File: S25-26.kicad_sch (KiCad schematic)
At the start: 122 parts, among them IC1 CMV4000-3E5M0PN, IC10 MT29F2G01ABAGDWB-IT_G_TR, IC13 DS90LV011AHMF_NOPB, IC2 XMC7200D-E272K8384AA, IC3 DS90LV048ATM_NOPB, IC4 DS90LV048ATM_NOPB, IC5 DS90LV048ATM_NOPB, IC6 NCV317BD2TR4G, IC7 MXL86110I-AQB-R, IC9 MT29F2G01ABAGDWB-IT_G_TR, J1 RJ45_RB1-125B8G1A, J2 DC_IN_PADS, J3 Conn_01x02_Pin, J4 Conn_01x04_Pin, Q2 ZXT849K, U1 TPS73601DBV, U2 TPS73601DBV, Y1 DSC1101DM2-012.0000

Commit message: Implementing Global Labels
Swapping generic I/O labels for global labels to help provide clarity in the schematic. Completed Supply Decoupling Caps, Temp. Sensing, Voltage Regulation, and part of Core Ext. Regulator
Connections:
- net DC_LINE_IN: no longer C36.1, Cin4.1, D1.1 (K), IC6.3 (VIN)
- net EXT_PS_CTL1 renamed XMC_VCCD
- new net DC_LINE_IN_28V: C36.1, Cin4.1, D1.1 (K), IC6.3 (VIN)
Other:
- moved on the sheet: C65, Q2, R2, R4, TR2, VCORE

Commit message: Reverted schematic to hierarchical structure.
The following connections are known to be floating:
FRAME_REQ
CMOS_RESET_N
CMOS_CLK_OUT
ETH0_RX_ER
ETH0_ETH_TSU_TIMER_CMP_VAL
ETH0_TX_ER
ETH0_REF_CLK
LVDS_RECV_EN
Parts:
- removed 2v1, 3v0, 3v3, VCORE, XRES: TestPoint, TestPoint:TestPoint_Pad_D1.0mm, symbol Connector:TestPoint
- removed C11, C14, C19, C20, C22: 0.1uF, symbol Device:C_Polarized
- removed C12, C17, C18, C21: 1nF, symbol Device:C_Polarized
- removed C13: 15pF, symbol Device:C
- removed C15: 0.1uF, symbol Device:C
- removed C16: 10uF, symbol Device:C_Small
- removed C23: 0.1F, symbol Device:C
- removed C36, CAdj4: 10uF, symbol Device:C_Polarized
- removed C37, C38, C39, C40, C41, C42, C44, C45, C46, C48, C49, C51, C52, C53, C54, C56, C59, C62, C64: 0.1uF, symbol Device:C_Small
- removed C43, C47, C50, C55, C58: 1uF, symbol Device:C_Small
- removed C57, C60: 10nF, symbol Device:C_Small
- removed C61, C63: 2.2uF, symbol Device:C_Small
- removed C65: 10uF, symbol Device:C
- removed CAdj5, CAdj6: 10nF, symbol Device:C_Polarized
- removed Cin4, Cin5, Cin6, Co4, Co5, Co6: 1uF, symbol Device:C_Polarized
- removed D1, D2: 1N4002, Diode_THT:D_DO-41_SOD81_P10.16mm_Horizontal, symbol Diode:1N4002
- removed IC10, IC9: MT29F2G01ABAGDWB-IT_G_TR, SON127P800X600X65-8N, symbol SamacSys_Parts:MT29F2G01ABAGDWB-IT_G_TR
- removed IC13: DS90LV011AHMF_NOPB, SOT95P280X145-5N, symbol SamacSys_Parts:DS90LV011AHMF_NOPB
- removed IC2: XMC7200D-E272K8384AA, BGA272C80P18X18_1600X1600X170, symbol SamacSys_Parts:XMC7200D-E272K8384AA
- removed IC3, IC4, IC5: DS90LV048ATM_NOPB, SOIC127P600X175-16N, symbol SamacSys_Parts:DS90LV048ATM_NOPB
- removed IC6: NCV317BD2TR4G, TO254P1420X457-4N, symbol SamacSys_Parts:NCV317BD2TR4G
- removed NT3, NT4: NetTie_2, symbol Device:NetTie_2
- removed Q2: ZXT849K, symbol Simulation_SPICE:NPN
- removed R4: 0.1, symbol Device:R
- removed RLVDS1, RLVDS13, RLVDS2, RLVDS3, RLVDS4, RLVDS5, RLVDS6, RLVDS7, RLVDS8, RLVDS9: 100, symbol Device:R_Small
- removed RP1_3: 164, symbol Device:R
- removed RP1_4, RP2_3: 100, symbol Device:R
- removed RP2_4: 150, symbol Device:R
- removed RP3_3: 120, symbol Device:R
- removed RP3_4: 90, symbol Device:R
- removed U1, U2: TPS73601DBV, Package_TO_SOT_SMD:SOT-23-5, symbol Regulator_Linear:TPS73601DBV
- removed Y1: DSC1101DM2-012.0000, DSC1101DM20120000, symbol SamacSys_Parts:DSC1101DM2-012.0000
- added NT1, NT2: NetTie_2, symbol Device:NetTie_2
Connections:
- net GNDSIG_A: now also NT2.1
- net GNDSIG_D: now also NT1.1
- net CMOS_CH01_N renamed LVDS Conversion/LVDS_CH01_N
- net CMOS_CH01_P renamed LVDS Conversion/LVDS_CH01_P
- net CMOS_CH03_N renamed LVDS Conversion/LVDS_CH03_N
- net CMOS_CH03_P renamed LVDS Conversion/LVDS_CH03_P
- net CMOS_CH05_N renamed LVDS Conversion/LVDS_CH05_N
- net CMOS_CH05_P renamed LVDS Conversion/LVDS_CH05_P
- net CMOS_CH07_N renamed LVDS Conversion/LVDS_CH07_N
- net CMOS_CH07_P renamed LVDS Conversion/LVDS_CH07_P
- net CMOS_CH09_N renamed LVDS Conversion/LVDS_CH09_N
- net CMOS_CH09_P renamed LVDS Conversion/LVDS_CH09_P
- net CMOS_CH11_N renamed LVDS Conversion/LVDS_CH11_N
- net CMOS_CH11_P renamed LVDS Conversion/LVDS_CH11_P
- net CMOS_CH13_N renamed LVDS Conversion/LVDS_CH13_N
- net CMOS_CH13_P renamed LVDS Conversion/LVDS_CH13_P
- net CMOS_CH15_N renamed LVDS Conversion/LVDS_CH15_N
- net CMOS_CH15_P renamed LVDS Conversion/LVDS_CH15_P
- net CMOS_CLK_OUT_N renamed LVDS Conversion/LVDS_CLK_OUT_N
- net CMOS_CLK_OUT_P renamed LVDS Conversion/LVDS_CLK_OUT_P
- net CMOS_CTR_OUT_N renamed LVDS Conversion/LVDS_CTR_OUT_N
- net CMOS_CTR_OUT_P renamed LVDS Conversion/LVDS_CTR_OUT_P
- net CMOS_LVDS_CLK_IN renamed CMOS_MASTER_CLK
- net DC_LINE_IN renamed Voltage Regulation/DC_LINE_IN_28V
- net GNDPWR renamed Voltage Regulation/GNDPWR
- net Voltage Regulation/GNDPWR: now also NT1.2, NT2.2
- net TEMPR_ADC0 renamed Processing/TEMPR_ADC0 (P6.0)
- net TEMPR_ADC1 renamed Processing/TEMPR_ADC1 (P6.1)
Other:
- added sheet LVDS Conversion (lvds.kicad_sch)
- added sheet Processing (processing.kicad_sch)
- added sheet Voltage Regulation (voltage_regulation.kicad_sch)
- note removed: "CMOS to LVDS Conversion"
- note removed: "Core External Regulator"
- note removed: "External Memory"
- note removed: "LVDS to CMOS Conversion"
- note removed: "Primary Microcontroller, Infineon XMC7200D"
- note removed: "Reference Oscillator"
- note removed: "Voltage Regulation"
- note removed: "XMC7200D Supply Decoupling Capacitors"
- moved on the sheet: C1, C10, C2, C26, C27, C28, C29, C3, C30, C31, C32, C33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

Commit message: One gnd to rule them all; PCB border (90 mm x 90 mm)
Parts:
- removed NT1, NT2: NetTie_2, symbol Device:NetTie_2
- J2: footprint Connector_Wire:SolderWire-0.1sqmm_1x02_P3.6mm_D0.4mm_OD1mm_Relief -> Connector_Wire:SolderWire-0.1sqmm_1x02_P3.6mm_D0.4mm_OD1mm
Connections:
- net GNDSIG_D is gone; now on net GND: IC7.41 (EP), J1.L2, J1.L4, J1.R10 (GND), R3.1
- net Voltage Regulation/GNDPWR is gone; now on net GND: J2.2
- net GNDSIG_A renamed GND
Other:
- sheet LVDS Conversion ports: added none; removed GNDSIG_A
- sheet Processing ports: added none; removed GNDSIG_A, GNDSIG_D
- sheet Voltage Regulation ports: added none; removed GNDPWR
- note removed: "Single-Point Connection between Analog and Digital Grounds"

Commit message: 3v3 Regulator routed; zones for 3v3 and gnd
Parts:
- IC1: footprint CMV40003E5M0PN -> SamacSys_Parts:CMV40003E5M0PN
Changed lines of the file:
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@@
 			)
 		)
-		(property "Footprint" "CMV40003E5M0PN"
+		(property "Footprint" "SamacSys_Parts:CMV40003E5M0PN"
 			(at 54.61 174.93 0)
 			(effects

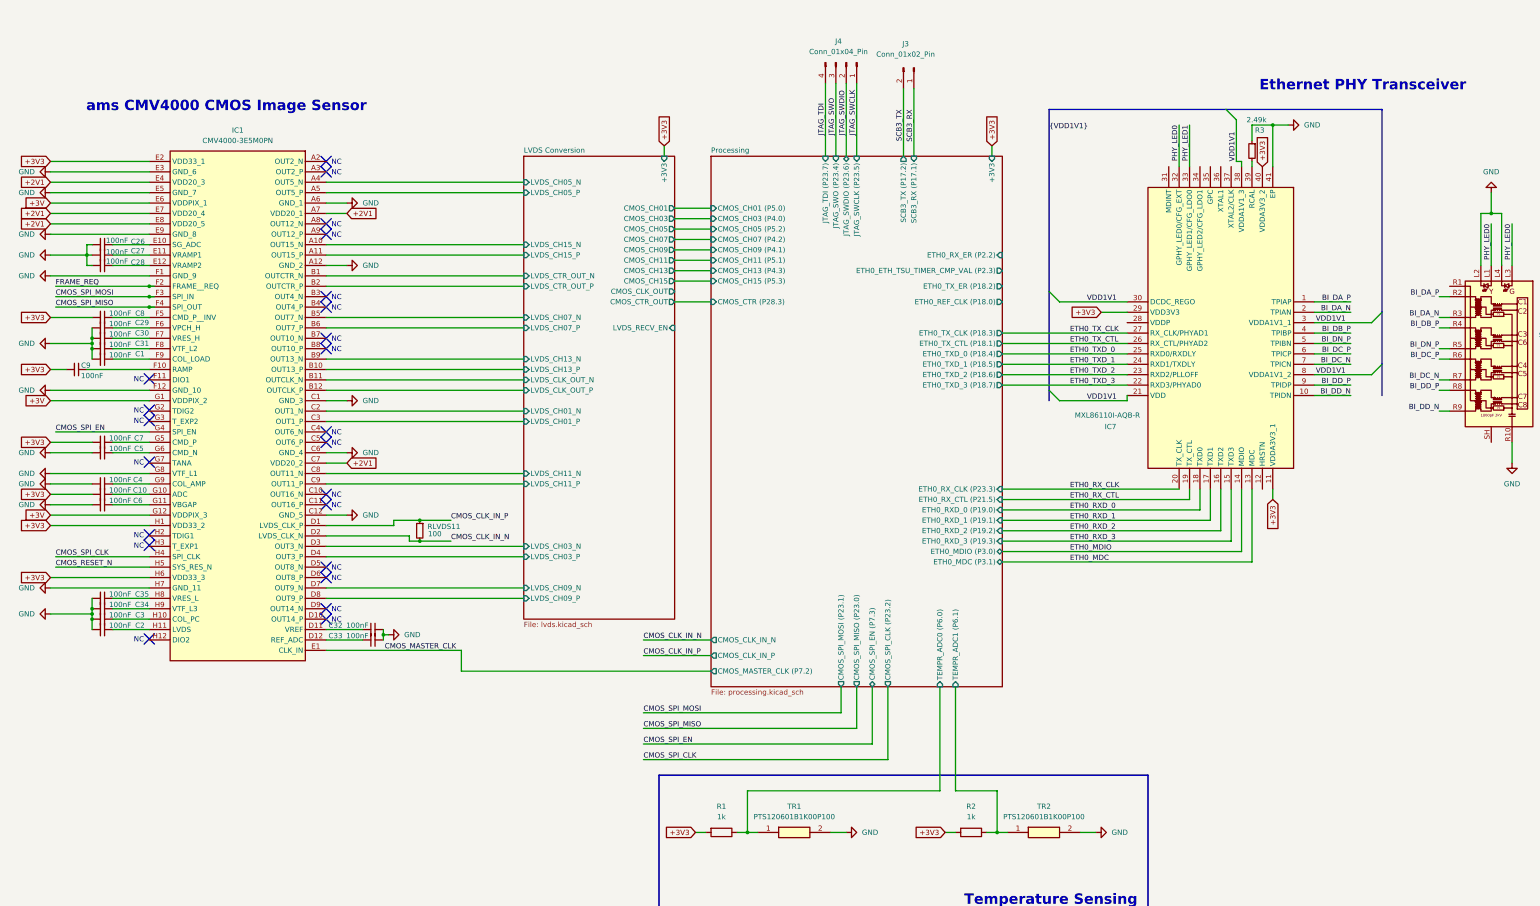
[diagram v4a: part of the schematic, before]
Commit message: Schematic - Component Specifics
Fixed floating connections.
Added parameters, footprints, Mouser part numbers, and Mouser links to all symbols, including discrete components and ICs.
The following symbols do not have Mouser part numbers or Mouser links:
CMOS Sensor (not required)
RJ45 Connector
JTAG Connector
DC Barrel Jack
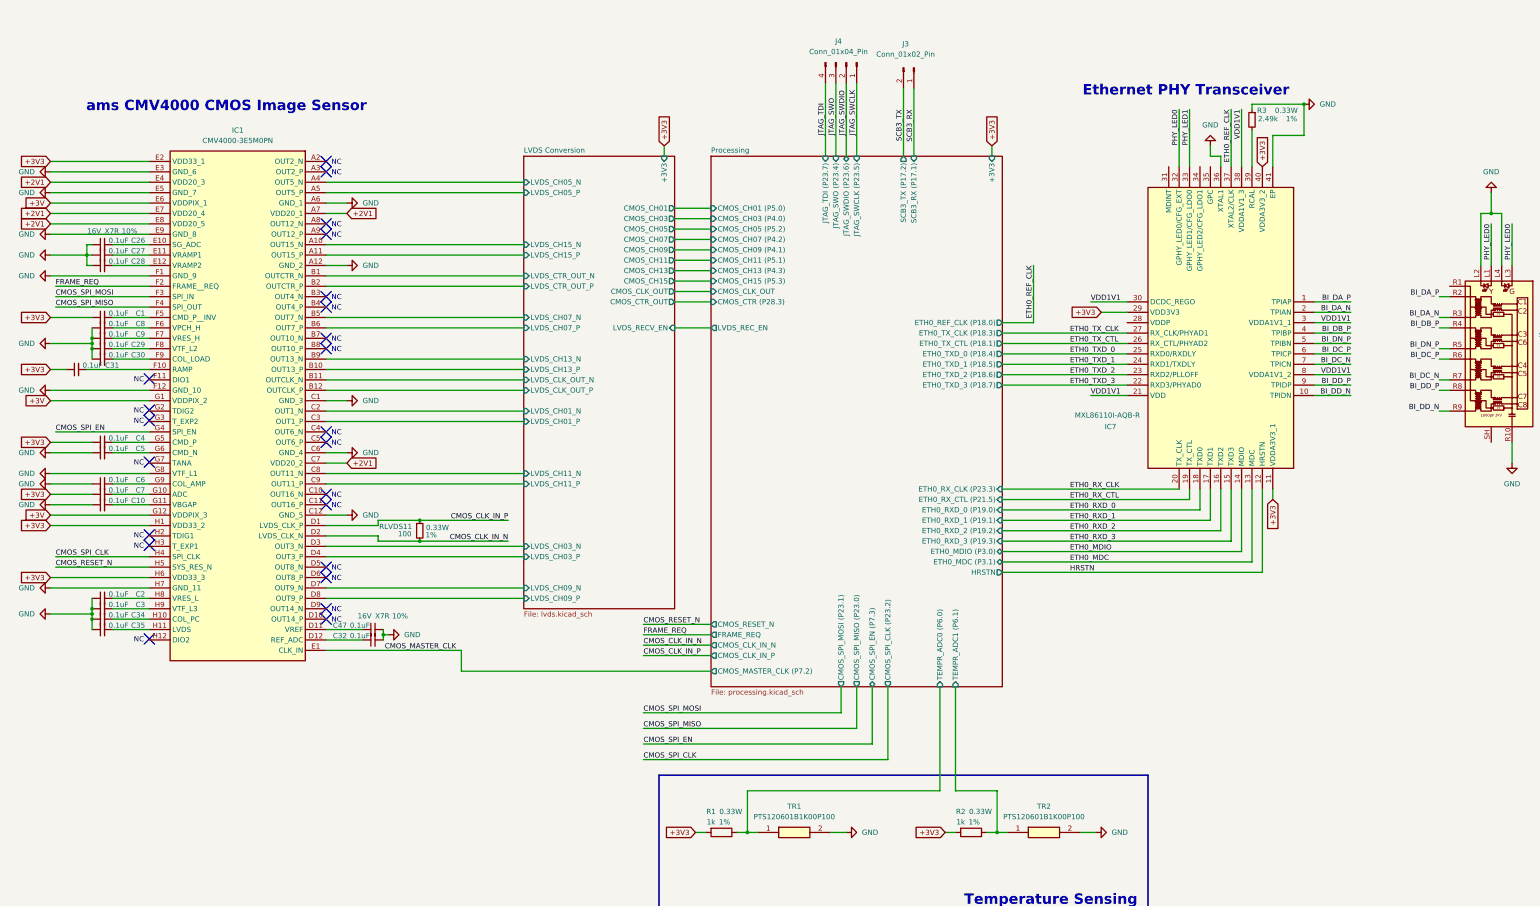
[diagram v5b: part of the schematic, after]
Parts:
- removed C33: 100nF, symbol Device:C_Small
- added C47: 0.1uF, Capacitor_SMD:C_0603_1608Metric, symbol Device:C_Small
- C1, C10, C2, C26, C27, C28, C29, C3, C30, C31, C32, C34, C35, C4, C5, C6, C7, C8, C9: value 100nF -> 0.1uF; footprint (none) -> Capacitor_SMD:C_0603_1608Metric; Dielectric (none) -> X7R; Mouser Part Number (none) -> 81-GCM188R71C104KA7J; Mouser Price/Stock (none) -> https://www.mouser.com/ProductDetail/Murata-Electronics/GCM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; Tolerance (none) -> 10%; Voltage Rating (none) -> 16V
- IC1: Arrow Part Number CMV4000-3E5M0PN -> (none); Arrow Price/Stock https://www.arrow.com/en/products/cmv4000-3e5m0pn/ams-ag?re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 -> (none)
- IC7: Arrow Part Number (none) -> 701-MXL86110I-AQB-R; Arrow Price/Stock (none) -> https://www.mouser.com/ProductDetail/MaxLinear/MXL86110I-AQ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
- R1, R2: footprint (none) -> Resistor_SMD:R_0603_1608Metric; Mouser Part Number (none) -> 71-CRCW06031K00FKED; Mouser Price/Stock (none) -> https://www.mouser.com/ProductDetail/Vishay-Dale/CRCW06031K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; Power Rating (none) -> 0.33W; Tolerance (none) -> 1%
- R3: footprint (none) -> Resistor_SMD:R_0603_1608Metric; Mouser Part Number (none) -> 71-CRCW06032K49FKEAH; Mouser Price/Stock (none) -> https://www.mouser.com/ProductDetail/Vishay-Dale/CRCW06032K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; Power Rating (none) -> 0.33W; Tolerance (none) -> 1%
- RLVDS11: footprint (none) -> Resistor_SMD:R_0603_1608Metric; Mouser Part Number (none) -> 71-CRCW0603100RFKEAH; Mouser Price/Stock (none) -> https://www.mouser.com/ProductDetail/Vishay-Dale/CRCW060310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; Power Rating (none) -> 0.33W; Tolerance (none) -> 1%
- TR1, TR2: Arrow Part Number PTS120601B1K00P100 -> (none); Arrow Price/Stock https://www.arrow.com/en/products/pts120601b1k00p100/vishay -> (none); Mouser Part Number (none) -> 594-PTS120601B1K00P; Mouser Price/Stock (none) -> https://www.mouser.com/ProductDetail/Vishay-Beyschlag/PTS12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
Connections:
- net +3V3: now also C1.1, C31.1, C4.1, C7.1; no longer C10.2, C7.2, C8.2, C9.2
- net GND: now also C10.1, C2.1, C26.1, C27.1, C28.1, C29.1, C3.1, C30.1, C34.1, C35.1, C5.1, C6.1, C8.1, C9.1, IC7.36 (XTAL1), C47.2; no longer C1.2, C2.2, C26.2, C27.2, C28.2, C29.2, C3.2, C30.2, C31.2, C34.2, C35.2, C4.2, C5.2, C6.2
- net at IC1.E11 (VRAMP1): now also C27.2; no longer C27.1
- net at IC1.G10 (ADC): now also C7.2; no longer C10.1
- net HRSTN: now reaches IC7.12 (HRSTN)
- net ETH0_REF_CLK: now reaches IC7.37 (XTAL2/CLK)
- net at IC1.G9 (COL_AMP): now also C6.2; no longer C4.1
- net at IC1.H9 (VTF_L3): now also C3.2; no longer C34.1
- net at IC1.F9 (COL_LOAD): now also C30.2; no longer C1.1
- net at IC1.E10 (SG_ADC): now also C26.2; no longer C26.1
- net at IC1.D11 (VREF): now also C47.1; no longer C32.1
- net at IC1.D12 (REF_ADC): now also C32.1
- net at IC1.E12 (VRAMP2): now also C28.2; no longer C28.1
- net at IC1.F10 (RAMP): now also C31.2; no longer C9.1
- net at IC1.F5 (CMD_P__INV): now also C1.2; no longer C8.1
- net at IC1.F6 (VPCH_H): now also C8.2; no longer C29.1
- net at IC1.F7 (VRES_H): now also C9.2; no longer C30.1
- net at IC1.F8 (VTF_L2): now also C29.2; no longer C31.1
- net at IC1.G11 (VBGAP): now also C10.2; no longer C6.1
- net at IC1.G5 (CMD_P): now also C4.2; no longer C7.1
- net at IC1.G6 (CMD_N): now also C5.2; no longer C5.1
- net at IC1.H10 (COL_PC): now also C34.2; no longer C3.1
- net at IC1.H11 (LVDS): now also C35.2; no longer C2.1
- net at IC1.H8 (VRES_L): now also C2.2; no longer C35.1
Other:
- sheet Processing ports: added CMOS_CLK_OUT, CMOS_RESET_N, FRAME_REQ, HRSTN, LVDS_REC_EN; removed ETH0_ETH_TSU_TIMER_CMP_VAL (P2.3), ETH0_RX_ER (P2.2), ETH0_TX_ER (P18.2)
- moved on the sheet: R3

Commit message: Some small changes for BOM
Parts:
- IC1, J2, J3, J4: now left out of the parts list
- IC7: Arrow Part Number 701-MXL86110I-AQB-R -> (none); Arrow Price/Stock https://www.mouser.com/ProductDetail/MaxLinear/MXL86110I-AQ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 -> (none); Mouser Part Number (none) -> 701-MXL86110I-AQB-R; Mouser Price/Stock (none) -> https://www.mouser.com/ProductDetail/MaxLinear/MXL86110I-AQ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
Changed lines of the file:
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@@
 			)
 		)
-		(property "Arrow Part Number" "701-MXL86110I-AQB-R"
+		(property "Mouser Part Number" "701-MXL86110I-AQB-R"
 			(at 293.37 783.82 0)
 			(effects
@@
 			)
 		)
-		(property "Arrow Price/Stock" "https://www.mouser.com/ProductDetail/MaxLinear/MXL86110I-AQB-R?qs=HoCaDK9Nz5dY9zcrCfZYZw%3D%3D"
+		(property "Mouser Price/Stock" "https://www.mouser.com/ProductDetail/MaxLinear/MXL86110I-AQB-R?qs=HoCaDK9Nz5dY9zcrCfZYZw%3D%3D"
 			(at 293.37 883.82 0)
 			(effects
@@
 		(unit 1)
 		(exclude_from_sim no)
-		(in_bom yes)
+		(in_bom no)
 		(on_board yes)
 		(dnp no)
@@
 		(unit 1)
 		(exclude_from_sim no)
-		(in_bom yes)
+		(in_bom no)
 		(on_board yes)
 		(dnp no)
@@
 		(unit 1)
 		(exclude_from_sim no)
-		(in_bom yes)
+		(in_bom no)
 		(on_board yes)
 		(dnp no)
@@
 		(unit 1)
 		(exclude_from_sim no)
-		(in_bom yes)
+		(in_bom no)
 		(on_board yes)
 		(dnp no)

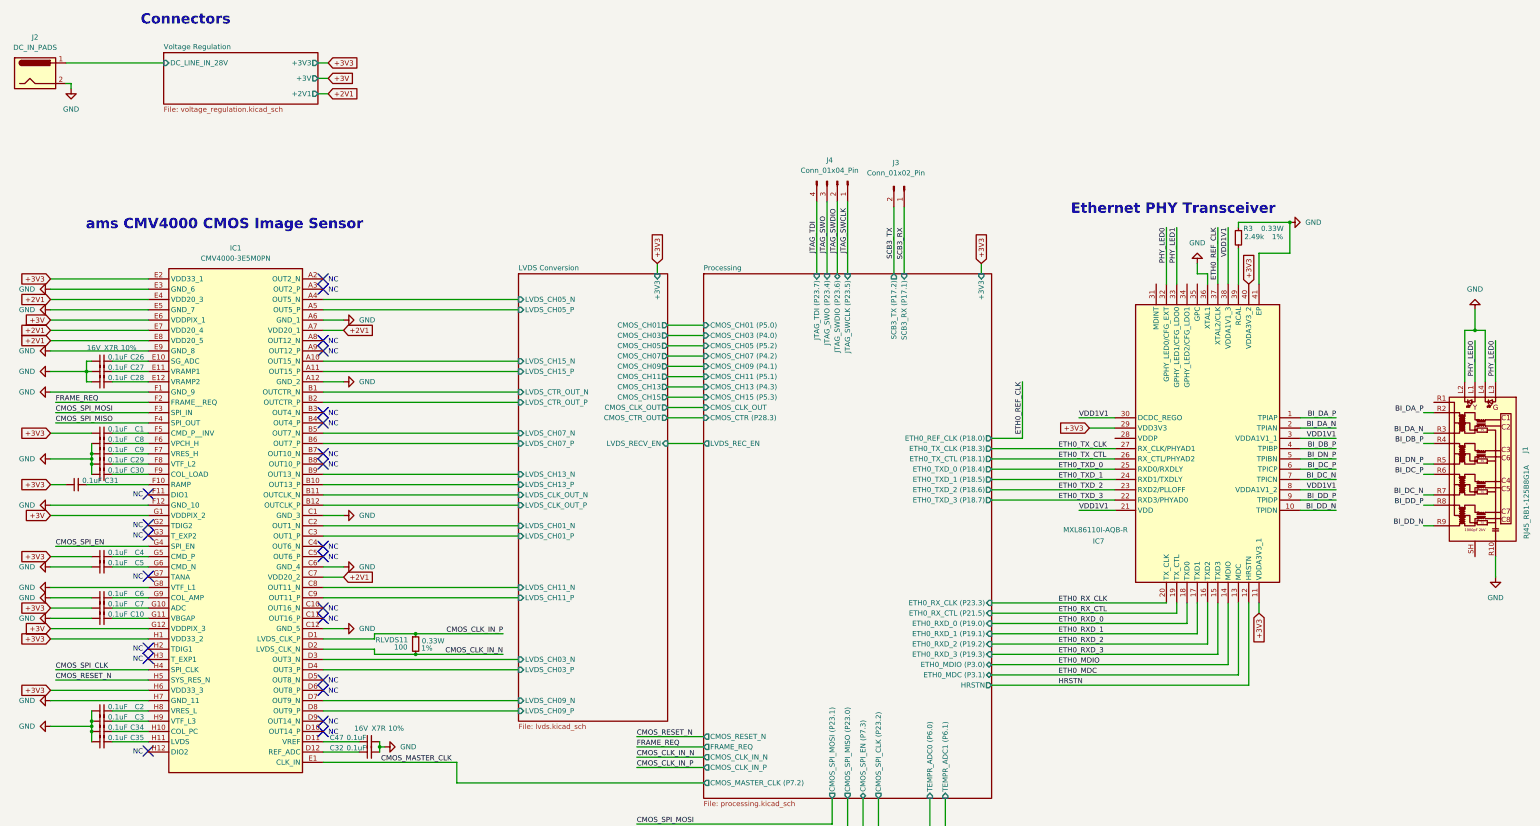
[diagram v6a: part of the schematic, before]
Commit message: Ethernet Transceiver
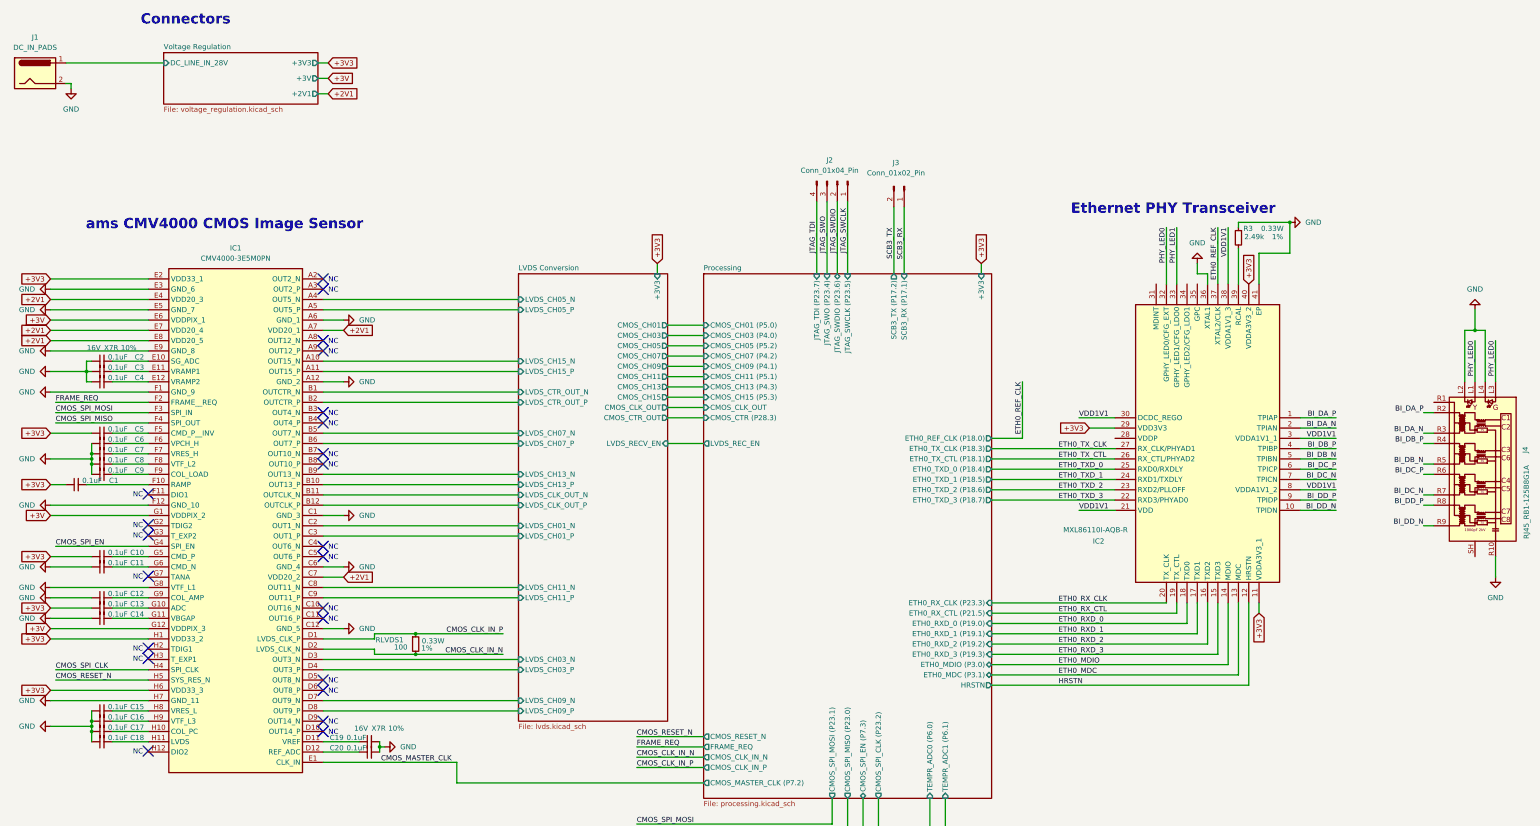
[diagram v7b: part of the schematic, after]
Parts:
- renumbered C31 to C1, C4 to C10, C5 to C11, C6 to C12, C7 to C13, C10 to C14, C2 to C15, C3 to C16, C34 to C17, C35 to C18, C47 to C19, C26 to C2, C32 to C20, C27 to C3, C28 to C4, C1 to C5, C8 to C6, C9 to C7, C29 to C8, C30 to C9, IC7 to IC2, J2 to J1, J4 to J2, J1 to J4, RLVDS11 to RLVDS1
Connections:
- net BI_DN_P renamed BI_DB_N
